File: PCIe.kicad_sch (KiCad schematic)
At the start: 0 parts

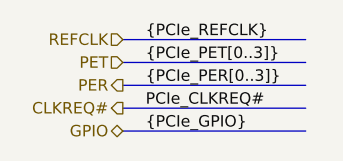
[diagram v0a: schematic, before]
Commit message: create netclass
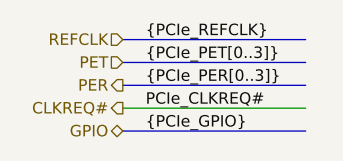
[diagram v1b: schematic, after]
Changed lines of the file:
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@@
+		)
+	)
+	(wire
+		(pts
+			(xy 121.92 81.28) (xy 142.24 81.28)
+		)
+		(stroke
+			(width 0)
+			(type default)
 		)
 	)
@@
 		)
 		(stroke
-			(width 0)
-			(type default)
-		)
-	)
-	(bus
-		(pts
-			(xy 142.24 81.28) (xy 121.92 81.28)
-		)
-		(stroke

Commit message: design CPU-RK3399 eMMC Controller
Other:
- company: (none) -> TickLab
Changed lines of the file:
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@@
 	(paper "A4")
 	(title_block
-		(date "2026-01-09")
+		(date "2026-01-14")
 		(rev "1.0.0")
+		(company "TickLab")
 	)
 	(bus_alias "PCIe_REFCLK"
